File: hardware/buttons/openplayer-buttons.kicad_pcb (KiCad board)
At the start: 2 copper layers, 14 x 116.1 mm, 10 parts, among them J1 CARRIER, SW1 POWER, SW2 VOL+, SW3 VOL-, SW4 PREV, SW5 PLAY, SW6 NEXT, SW7 MENU

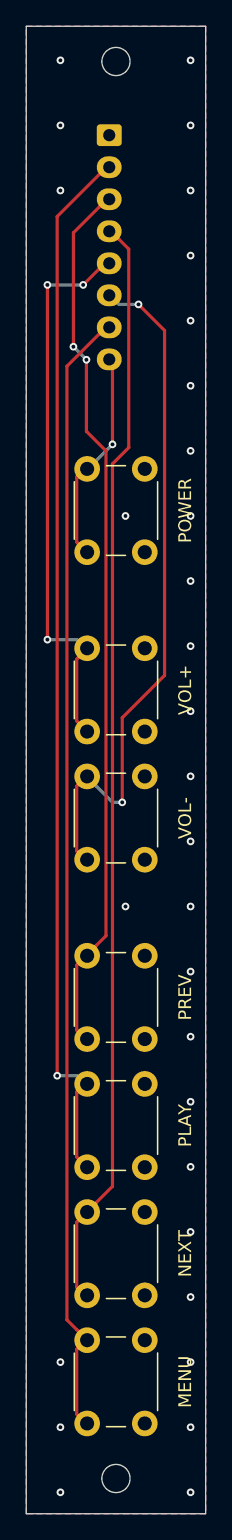
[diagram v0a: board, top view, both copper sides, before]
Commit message: Refactor button layout and update PCB design for OpenPlayer Rev B
- Adjusted button pitch to 9.6 mm for improved spacing.
- Modified button group configuration to exclude SW1 and clarify power connection.
- Updated pin labels to reflect unused pin 8 as "NC" for clarity.
- Changed silkscreen text to indicate revision B.
- Enhanced net handling to include unconnected pins for better design integrity.
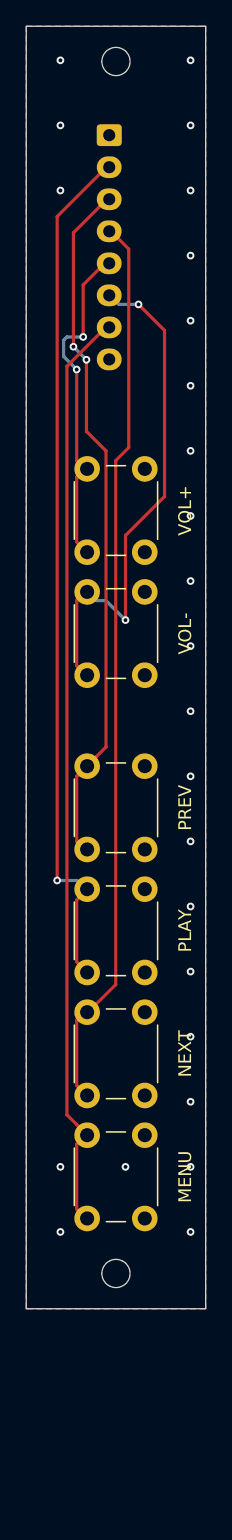
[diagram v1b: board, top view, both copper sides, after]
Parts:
- removed SW1: POWER, Button_Switch_THT:SW_PUSH_6mm
- moved H2 16.0 mm to (107.0, 197.3)
- moved SW7 16.0 mm to (104.8, 193.0)
- moved SW6 15.6 mm to (104.8, 183.4)
- moved SW5 15.2 mm to (104.8, 173.8)
- moved SW4 14.8 mm to (104.8, 164.2)
- moved SW3 14.4 mm to (104.8, 150.6)
- moved SW2 14.0 mm to (104.8, 141.0)
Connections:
- J1 pad 8: /PWR_KEY -> unconnected-(J1-Pin_8-Pad8)
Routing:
- net /BTN_VOLUP: track 43.7 -> 26.5 mm, vias 3 -> 2
- net /PWR_KEY: track 16.7 -> 0.00 mm, vias 1 -> 0
- net /BTN_MENU: track 88.4 -> 72.4 mm
- net /BTN_NEXT: track 85.8 -> 70.2 mm
- net /BTN_PLAY: track 82.5 -> 67.2 mm
- net /BTN_PREV: track 69.1 -> 54.4 mm
- net /BTN_VOLDN: track 54.5 -> 40.4 mm
- net /GND: vias 31 -> 25
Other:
- board size 14 x 116.1 mm -> 14 x 100.1 mm
- board text added: "NC"
- board text added: "OpenPlayer buttons Rev B"
- board text removed: "KEY"
- board text removed: "OpenPlayer buttons Rev A"
- board text removed: "POWER"
